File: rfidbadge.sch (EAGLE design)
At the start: 49 parts, among them Q1 BSS123, U1 ATMEGA328P_TQFP, U2 CLRC663, Y1 27.12 MHz

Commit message: Finish routing
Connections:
- removed net VSS: FTDI.3, U2.IFSEL1
- net GND: now also U2.IFSEL1
- net VDD: now also FTDI.3
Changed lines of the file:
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@@
 <wire x1="91.44" y1="71.12" x2="91.44" y2="68.58" width="0.1524" layer="91"/>
+</segment>
+<segment>
+<pinref part="U2" gate="G$1" pin="IFSEL1"/>
+<wire x1="68.58" y1="7.62" x2="66.04" y2="7.62" width="0.1524" layer="91"/>
+<label x="66.04" y="7.62" size="1.778" layer="95" rot="R180"/>
 </segment>
 </net>
@@
 <junction x="50.8" y="-27.94"/>
 </segment>
+<segment>
+<pinref part="FTDI" gate="A" pin="3"/>
+<wire x1="30.48" y1="-53.34" x2="22.86" y2="-53.34" width="0.1524" layer="91"/>
+<label x="22.86" y="-53.34" size="1.778" layer="95" rot="R180"/>
+</segment>
 </net>
 <net name="TVDD" class="0">
@@
 </segment>
 </net>
-<net name="VSS" class="0">
-<segment>
-<pinref part="U2" gate="G$1" pin="IFSEL1"/>
-<wire x1="68.58" y1="7.62" x2="66.04" y2="7.62" width="0.1524" layer="91"/>
-<label x="66.04" y="7.62" size="1.778" layer="95" rot="R180"/>
-</segment>
-<segment>
-<pinref part="FTDI" gate="A" pin="3"/>
-<wire x1="30.48" y1="-53.34" x2="22.86" y2="-53.34" width="0.1524" layer="91"/>
-<label x="22.86" y="-53.34" size="1.778" layer="95" rot="R180"/>
-</segment>
-</net>

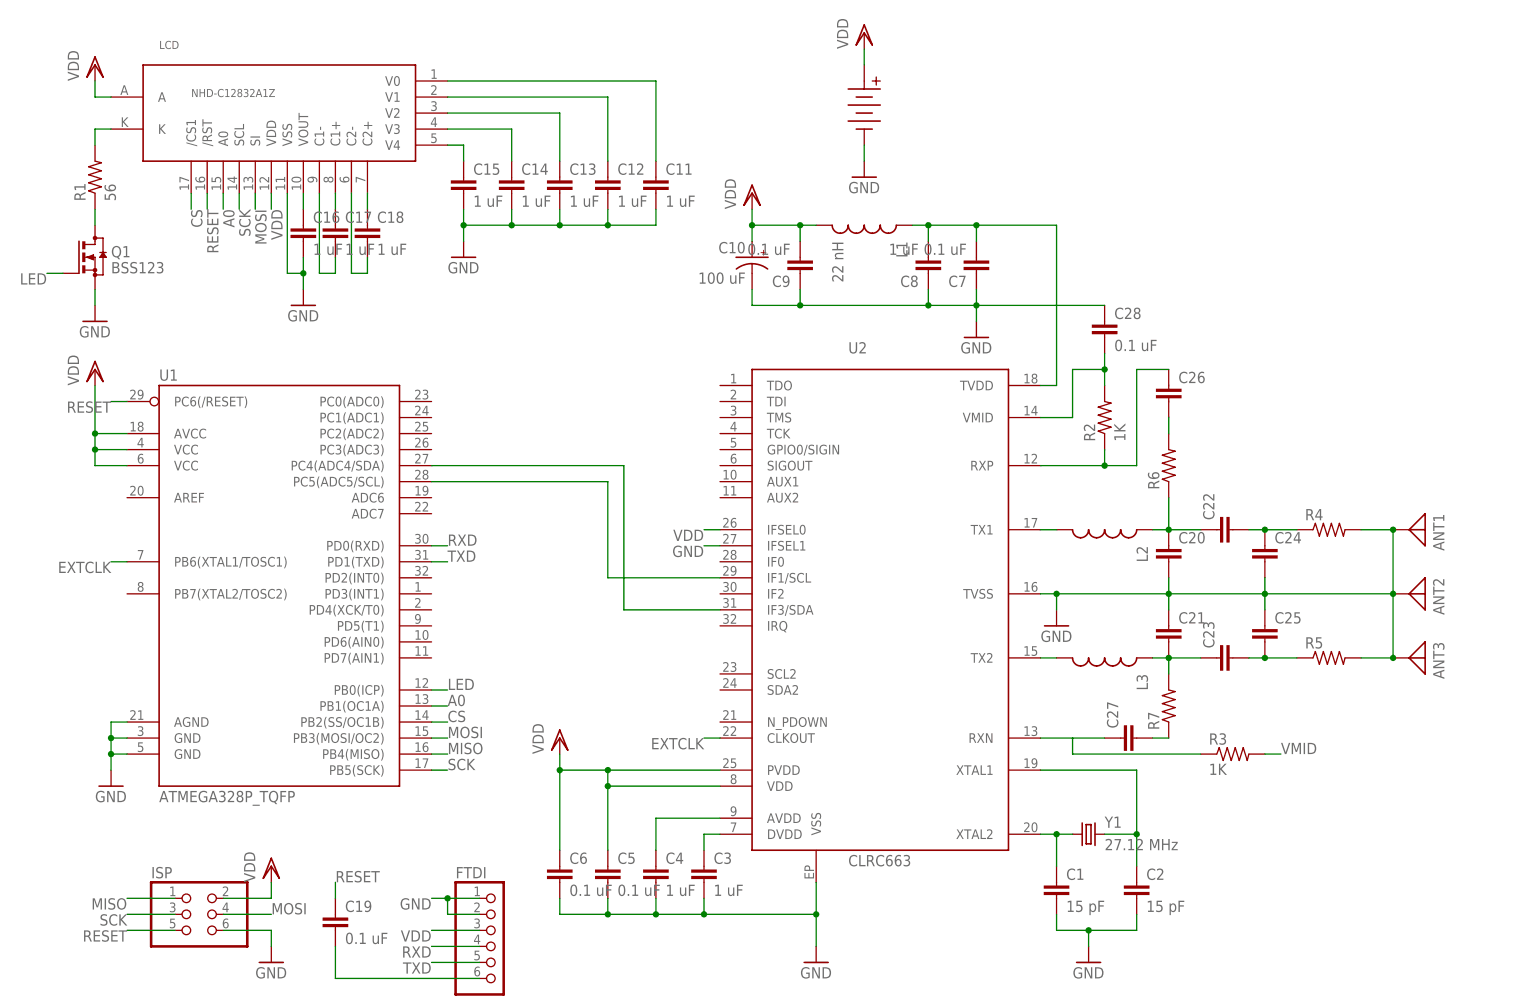
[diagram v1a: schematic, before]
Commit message: Add switches, lanyard holes, rounded corners
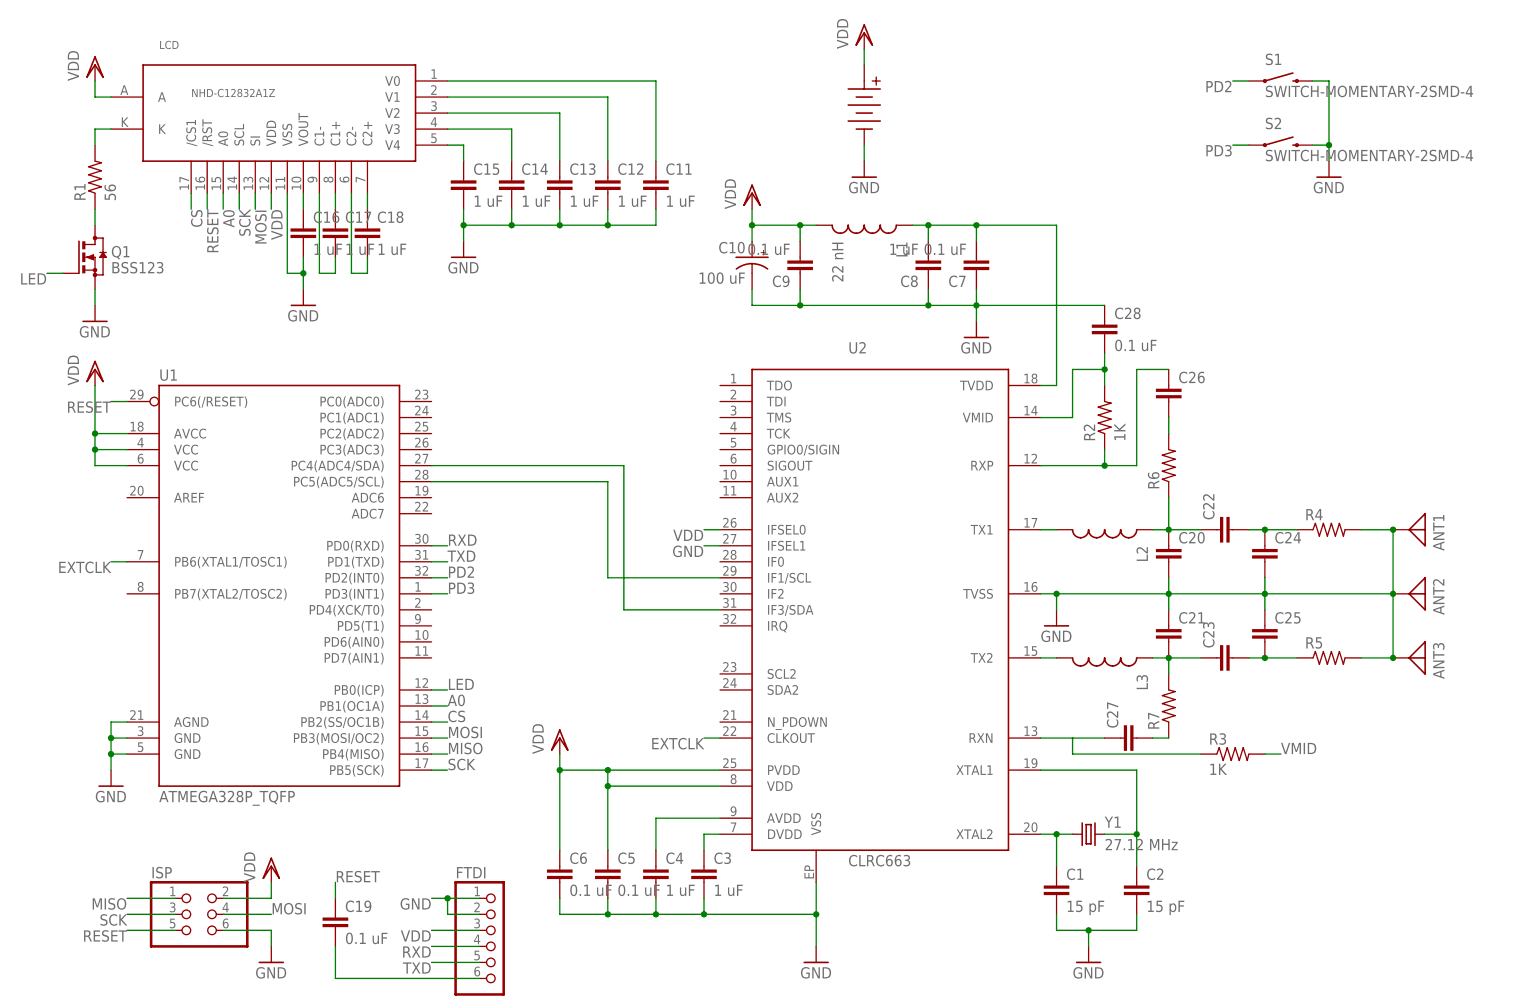
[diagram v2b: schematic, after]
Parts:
- added S1, S2: SWITCH-MOMENTARY-2SMD-4, SparkFun-Electromechanical:SWITCH-MOMENTARY-2SMD-4
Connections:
- new net PD2: S1.1, U1.PD2(INT0)
- new net PD3: S2.1, U1.PD3(INT1)
- net GND: now also S1.2, S2.2
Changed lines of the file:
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@@
 <part name="GND10" library="supply1" deviceset="GND" device=""/>
 <part name="VDD6" library="supply1" deviceset="VDD" device=""/>
+<part name="S1" library="SparkFun-Electromechanical" deviceset="SWITCH-MOMENTARY-2" device="SMD-4"/>
+<part name="S2" library="SparkFun-Electromechanical" deviceset="SWITCH-MOMENTARY-2" device="SMD-4"/>
+<part name="GND11" library="supply1" deviceset="GND" device=""/>
 </parts>
 <sheets>
@@
 <instance part="GND10" gate="1" x="91.44" y="66.04"/>
 <instance part="VDD6" gate="G$1" x="91.44" y="88.9"/>
+<instance part="S1" gate="G$1" x="157.48" y="81.28"/>
+<instance part="S2" gate="G$1" x="157.48" y="71.12"/>
+<instance part="GND11" gate="1" x="165.1" y="66.04"/>
 </instances>
 <busses>
@@
 <label x="66.04" y="7.62" size="1.778" layer="95" rot="R180"/>
 </segment>
+<segment>
+<pinref part="S1" gate="G$1" pin="2"/>
+<pinref part="GND11" gate="1" pin="GND"/>
+<wire x1="162.56" y1="81.28" x2="165.1" y2="81.28" width="0.1524" layer="91"/>
+<wire x1="165.1" y1="81.28" x2="165.1" y2="71.12" width="0.1524" layer="91"/>
+<pinref part="S2" gate="G$1" pin="2"/>
+<wire x1="165.1" y1="71.12" x2="165.1" y2="68.58" width="0.1524" layer="91"/>
+<wire x1="162.56" y1="71.12" x2="165.1" y2="71.12" width="0.1524" layer="91"/>
+<junction x="165.1" y="71.12"/>
+</segment>
 </net>
 <net name="EXTCLK" class="0">
@@
 </segment>
 </net>
+<net name="PD2" class="0">
+<segment>
+<pinref part="U1" gate="U$1" pin="PD2(INT0)"/>
+<wire x1="22.86" y1="2.54" x2="25.4" y2="2.54" width="0.1524" layer="91"/>
+<label x="25.4" y="2.54" size="1.778" layer="95"/>
+</segment>
+<segment>
+<pinref part="S1" gate="G$1" pin="1"/>
+<wire x1="152.4" y1="81.28" x2="149.86" y2="81.28" width="0.1524" layer="91"/>
+<label x="149.86" y="81.28" size="1.778" layer="95" rot="R180"/>
+</segment>
+</net>
+<net name="PD3" class="0">
+<segment>
+<pinref part="U1" gate="U$1" pin="PD3(INT1)"/>
+<wire x1="22.86" y1="0" x2="25.4" y2="0" width="0.1524" layer="91"/>
+<label x="25.4" y="0" size="1.778" layer="95"/>
+</segment>
+<segment>
+<pinref part="S2" gate="G$1" pin="1"/>
+<wire x1="152.4" y1="71.12" x2="149.86" y2="71.12" width="0.1524" layer="91"/>
+<label x="149.86" y="71.12" size="1.778" layer="95" rot="R180"/>
+</segment>
+</net>

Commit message: Added some test pads
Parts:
- added TP1, TP2, TP3, TP4, TP5, TP6: TPTP06R, testpad:TPTP06R
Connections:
- new net N$12: TP3.TP, U2.TMS
- new net N$13: TP4.TP, U2.TCK
- new net N$14: TP5.TP, U2.GPIO0/SIGIN
- new net N$15: TP6.TP, U2.SIGOUT
- new net N$5: TP1.TP, U2.TDO
- new net N$6: TP2.TP, U2.TDI
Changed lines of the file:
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@@
 <part name="S2" library="SparkFun-Electromechanical" deviceset="SWITCH-MOMENTARY-2" device="SMD-4"/>
 <part name="GND11" library="supply1" deviceset="GND" device=""/>
+<part name="TP1" library="testpad" deviceset="TP" device="TP06R" value="TPTP06R"/>
+<part name="TP2" library="testpad" deviceset="TP" device="TP06R" value="TPTP06R"/>
+<part name="TP3" library="testpad" deviceset="TP" device="TP06R" value="TPTP06R"/>
+<part name="TP4" library="testpad" deviceset="TP" device="TP06R" value="TPTP06R"/>
+<part name="TP5" library="testpad" deviceset="TP" device="TP06R" value="TPTP06R"/>
+<part name="TP6" library="testpad" deviceset="TP" device="TP06R" value="TPTP06R"/>
 </parts>
 <sheets>
@@
 <instance part="S2" gate="G$1" x="157.48" y="71.12"/>
 <instance part="GND11" gate="1" x="165.1" y="66.04"/>
+<instance part="TP1" gate="G$1" x="63.5" y="33.02" rot="R90"/>
+<instance part="TP2" gate="G$1" x="63.5" y="30.48" rot="R90"/>
+<instance part="TP3" gate="G$1" x="63.5" y="27.94" rot="R90"/>
+<instance part="TP4" gate="G$1" x="63.5" y="25.4" rot="R90"/>
+<instance part="TP5" gate="G$1" x="63.5" y="22.86" rot="R90"/>
+<instance part="TP6" gate="G$1" x="63.5" y="20.32" rot="R90"/>
 </instances>
 <busses>
@@
 </segment>
 </net>
+<net name="N$5" class="0">
+<segment>
+<pinref part="U2" gate="G$1" pin="TDO"/>
+<wire x1="66.04" y1="33.02" x2="68.58" y2="33.02" width="0.1524" layer="91"/>
+<pinref part="TP1" gate="G$1" pin="TP"/>
+</segment>
+</net>
+<net name="N$6" class="0">
+<segment>
+<pinref part="U2" gate="G$1" pin="TDI"/>
+<wire x1="68.58" y1="30.48" x2="66.04" y2="30.48" width="0.1524" layer="91"/>
+<pinref part="TP2" gate="G$1" pin="TP"/>
+</segment>
+</net>
+<net name="N$12" class="0">
+<segment>
+<pinref part="U2" gate="G$1" pin="TMS"/>
+<wire x1="68.58" y1="27.94" x2="66.04" y2="27.94" width="0.1524" layer="91"/>
+<pinref part="TP3" gate="G$1" pin="TP"/>
+</segment>
+</net>
+<net name="N$13" class="0">
+<segment>
+<pinref part="U2" gate="G$1" pin="TCK"/>
+<wire x1="68.58" y1="25.4" x2="66.04" y2="25.4" width="0.1524" layer="91"/>
+<pinref part="TP4" gate="G$1" pin="TP"/>
+</segment>
+</net>
+<net name="N$14" class="0">
+<segment>
+<pinref part="U2" gate="G$1" pin="GPIO0/SIGIN"/>
+<wire x1="68.58" y1="22.86" x2="66.04" y2="22.86" width="0.1524" layer="91"/>
+<pinref part="TP5" gate="G$1" pin="TP"/>
+</segment>
+</net>
+<net name="N$15" class="0">
+<segment>
+<pinref part="U2" gate="G$1" pin="SIGOUT"/>
+<wire x1="68.58" y1="20.32" x2="66.04" y2="20.32" width="0.1524" layer="91"/>
+<pinref part="TP6" gate="G$1" pin="TP"/>
+</segment>
+</net>

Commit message: Some part values
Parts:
- C20, C21, C26, C27: PROD_ID 311-1060-1-ND -> (none)
- C22, C23: value (none) -> 56 pF; PROD_ID 311-1060-1-ND -> 445-1278-1-ND
- C24, C25: value (none) -> 820 pF; PROD_ID 311-1060-1-ND -> 445-1292-1-ND
- R4, R5: value (none) -> 0.39; PROD_ID (none) -> P.39AHCT-ND
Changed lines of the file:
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@@
 <part name="L3" library="SparkFun-Passives" deviceset="INDUCTOR" device="30OHM,1.8A"/>
 <part name="C20" library="rcl" deviceset="C-EU" device="C0603K">
-<attribute name="PROD_ID" value="311-1060-1-ND"/>
+<attribute name="PROD_ID" value=""/>
 </part>
 <part name="C21" library="rcl" deviceset="C-EU" device="C0603K">
-<attribute name="PROD_ID" value="311-1060-1-ND"/>
+<attribute name="PROD_ID" value=""/>
 </part>
-<part name="C22" library="rcl" deviceset="C-EU" device="C0603K">
-<attribute name="PROD_ID" value="311-1060-1-ND"/>
+<part name="C22" library="rcl" deviceset="C-EU" device="C0603K" value="56 pF">
+<attribute name="PROD_ID" value="445-1278-1-ND"/>
 </part>
-<part name="C23" library="rcl" deviceset="C-EU" device="C0603K">
-<attribute name="PROD_ID" value="311-1060-1-ND"/>
+<part name="C23" library="rcl" deviceset="C-EU" device="C0603K" value="56 pF">
+<attribute name="PROD_ID" value="445-1278-1-ND"/>
 </part>
-<part name="C24" library="rcl" deviceset="C-EU" device="C0603K">
-<attribute name="PROD_ID" value="311-1060-1-ND"/>
+<part name="C24" library="rcl" deviceset="C-EU" device="C0603K" value="820 pF">
+<attribute name="PROD_ID" value="445-1292-1-ND"/>
 </part>
-<part name="C25" library="rcl" deviceset="C-EU" device="C0603K">
-<attribute name="PROD_ID" value="311-1060-1-ND"/>
+<part name="C25" library="rcl" deviceset="C-EU" device="C0603K" value="820 pF">
+<attribute name="PROD_ID" value="445-1292-1-ND"/>
 </part>
-<part name="R4" library="rcl" deviceset="R-US_" device="R0603"/>
-<part name="R5" library="rcl" deviceset="R-US_" device="R0603"/>
+<part name="R4" library="rcl" deviceset="R-US_" device="R0603" value="0.39">
+<attribute name="PROD_ID" value="P.39AHCT-ND"/>
+</part>
+<part name="R5" library="rcl" deviceset="R-US_" device="R0603" value="0.39">
+<attribute name="PROD_ID" value="P.39AHCT-ND"/>
+</part>
 <part name="ANT1" library="discrete" deviceset="ANTENNA" device=""/>
 <part name="ANT2" library="discrete" deviceset="ANTENNA" device=""/>
@@
 <part name="R7" library="rcl" deviceset="R-US_" device="R0603"/>
 <part name="C26" library="rcl" deviceset="C-EU" device="C0603K">
-<attribute name="PROD_ID" value="311-1060-1-ND"/>
+<attribute name="PROD_ID" value=""/>
 </part>
 <part name="C27" library="rcl" deviceset="C-EU" device="C0603K">
-<attribute name="PROD_ID" value="311-1060-1-ND"/>
+<attribute name="PROD_ID" value=""/>
 </part>
 <part name="C28" library="rcl" deviceset="C-EU" device="C0603K" value="0.1 uF">
@@
 <attribute name="PROD_ID" x="154.94" y="-5.08" size="1.778" layer="96" display="off"/>
 </instance>
-<instance part="R4" gate="G$1" x="165.1" y="10.16"/>
-<instance part="R5" gate="G$1" x="165.1" y="-10.16"/>
+<instance part="R4" gate="G$1" x="165.1" y="10.16">
+<attribute name="PROD_ID" x="165.1" y="10.16" size="1.778" layer="96" display="off"/>
+</instance>
+<instance part="R5" gate="G$1" x="165.1" y="-10.16">
+<attribute name="PROD_ID" x="165.1" y="-10.16" size="1.778" layer="96" display="off"/>
+</instance>
 <instance part="ANT1" gate="A" x="180.34" y="10.16" rot="R270"/>
 <instance part="ANT2" gate="A" x="180.34" y="0" rot="R270"/>
